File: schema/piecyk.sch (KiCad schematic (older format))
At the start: 19 parts, among them IC1 ATMEGA8A-P, Q1 PNP, SW1 SW_edit, SW2 SW_down, SW3 SW_up, U1 78L05, U2 LM35

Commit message: Correct schematics (NPN instead of PNP)
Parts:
- removed Q1: PNP, ~, symbol PNP
- added Q1: NPN, ~, symbol NPN
- added R5: R, ~, symbol R
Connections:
- net labels added: +12V / heating -
- wire segments 78 -> 82
- no-connect marks 14 -> 13
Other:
- moved on the sheet: D1, R2
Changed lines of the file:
@@
 LIBS:display_lcd
 LIBS:capteurs
-LIBS:noname-cache
 EELAYER 27 0
 EELAYER END
@@
 Vcc +5V
 $Comp
-L PNP Q1
-U 1 1 52D0DFF4
-P 6950 5500
-F 0 "Q1" H 6950 5350 60  0000 R CNN
-F 1 "PNP" H 6950 5650 60  0000 R CNN
-F 2 "~" H 6950 5500 60  0000 C CNN
-F 3 "~" H 6950 5500 60  0000 C CNN
-	1    6950 5500
-	-1   0    0    1
-$EndComp
-$Comp
 L LED D1
 U 1 1 52D0E01F
-P 7100 4700
-F 0 "D1" H 7100 4800 50  0000 C CNN
-F 1 "LED" H 7100 4600 50  0000 C CNN
-F 2 "~" H 7100 4700 60  0000 C CNN
-F 3 "~" H 7100 4700 60  0000 C CNN
-	1    7100 4700
+P 7400 4850
+F 0 "D1" H 7400 4950 50  0000 C CNN
+F 1 "LED" H 7400 4750 50  0000 C CNN
+F 2 "~" H 7400 4850 60  0000 C CNN
+F 3 "~" H 7400 4850 60  0000 C CNN
+	1    7400 4850
 	1    0    0    -1
 $EndComp
@@
 L R R2
 U 1 1 52D0E03F
-P 7300 5250
-F 0 "R2" V 7380 5250 40  0000 C CNN
-F 1 "R" V 7307 5251 40  0000 C CNN
-F 2 "~" V 7230 5250 30  0000 C CNN
-F 3 "~" H 7300 5250 30  0000 C CNN
-	1    7300 5250
+P 8200 4450
+F 0 "R2" V 8280 4450 40  0000 C CNN
+F 1 "R" V 8207 4451 40  0000 C CNN
+F 2 "~" V 8130 4450 30  0000 C CNN
+F 3 "~" H 8200 4450 30  0000 C CNN
+	1    8200 4450
 	-1   0    0    1
-$EndComp
-Text GLabel 7200 6100 2    60   Output ~ 0
-+12V piec
-$Comp
-L +12V #PWR09
-U 1 1 52D0E282
-P 6850 5100
-F 0 "#PWR09" H 6850 5050 20  0001 C CNN
-F 1 "+12V" H 6850 5200 30  0000 C CNN
-F 2 "" H 6850 5100 60  0000 C CNN
-F 3 "" H 6850 5100 60  0000 C CNN
-	1    6850 5100
-	1    0    0    -1
 $EndComp
 $Comp
@@
 $EndComp
 $Comp
-L GND #PWR010
+L GND #PWR09
 U 1 1 52D0F85C
 P 8650 2900
-F 0 "#PWR010" H 8650 2900 30  0001 C CNN
+F 0 "#PWR09" H 8650 2900 30  0001 C CNN
 F 1 "GND" H 8650 2830 30  0001 C CNN
 F 2 "" H 8650 2900 60  0000 C CNN
@@
 $EndComp
 $Comp
-L GND #PWR011
+L GND #PWR010
 U 1 1 52D0F869
 P 10550 2900
-F 0 "#PWR011" H 10550 2900 30  0001 C CNN
+F 0 "#PWR010" H 10550 2900 30  0001 C CNN
 F 1 "GND" H 10550 2830 30  0001 C CNN
 F 2 "" H 10550 2900 60  0000 C CNN
@@
 $EndComp
 $Comp
-L GND #PWR012
+L GND #PWR011
 U 1 1 52D0FAD8
 P 5750 4350
-F 0 "#PWR012" H 5750 4350 30  0001 C CNN
+F 0 "#PWR011" H 5750 4350 30  0001 C CNN
 F 1 "GND" H 5750 4280 30  0001 C CNN
 F 2 "" H 5750 4350 60  0000 C CNN
@@
 	3600 6450 3600 6600
 Wire Wire Line
-	7200 6100 6850 6100
-Wire Wire Line
-	6850 6100 6850 5700
-Wire Wire Line
-	6850 5100 6850 5300
-Wire Wire Line
-	7300 5500 7150 5500
-Wire Wire Line
 	1550 3000 6700 3000
 Wire Wire Line
@@
 Connection ~ 6450 5650
 Wire Wire Line
-	7300 4700 7300 5000
-Wire Wire Line
 	4600 5250 5250 5250
 Wire Wire Line
 	5250 5250 5250 4700
-Wire Wire Line
-	5250 4700 6900 4700
 Wire Wire Line
 	9350 2250 9350 1700
@@
 NoConn ~ 4600 4950
 NoConn ~ 4600 5050
-NoConn ~ 4600 5350
 NoConn ~ 9450 2250
 NoConn ~ 9550 2250
@@
 NoConn ~ 9750 2250
 $Comp
-L GND #PWR013
+L GND #PWR012
 U 1 1 52D0FA8D
 P 9450 6100
-F 0 "#PWR013" H 9450 6100 30  0001 C CNN
+F 0 "#PWR012" H 9450 6100 30  0001 C CNN
 F 1 "GND" H 9450 6030 30  0001 C CNN
 F 2 "" H 9450 6100 60  0000 C CNN
@@
 $EndComp
 $Comp
-L +12V #PWR014
+L +12V #PWR013
 U 1 1 52D0FA9C
 P 9650 5650
-F 0 "#PWR014" H 9650 5600 20  0001 C CNN
+F 0 "#PWR013" H 9650 5600 20  0001 C CNN
 F 1 "+12V" H 9650 5750 30  0000 C CNN
 F 2 "" H 9650 5650 60  0000 C CNN
@@
 +12V piec
 $Comp
-L PWR_FLAG #FLG015
+L PWR_FLAG #FLG014
 U 1 1 52D0FAAD
 P 9450 5700
-F 0 "#FLG015" H 9450 5795 30  0001 C CNN
+F 0 "#FLG014" H 9450 5795 30  0001 C CNN
 F 1 "PWR_FLAG" H 9450 5880 30  0000 C CNN
 F 2 "" H 9450 5700 60  0000 C CNN
@@
 $EndComp
 $Comp
-L PWR_FLAG #FLG016
+L PWR_FLAG #FLG015
 U 1 1 52D0FAC7
 P 9650 6000
-F 0 "#FLG016" H 9650 6095 30  0001 C CNN
+F 0 "#FLG015" H 9650 6095 30  0001 C CNN
 F 1 "PWR_FLAG" H 9650 6180 30  0000 C CNN
 F 2 "" H 9650 6000 60  0000 C CNN
@@
 	9450 5700 9450 6100
 $Comp
-L PWR_FLAG #FLG017
+L PWR_FLAG #FLG016
 U 1 1 52D0FB94
 P 9850 5700
-F 0 "#FLG017" H 9850 5795 30  0001 C CNN
+F 0 "#FLG016" H 9850 5795 30  0001 C CNN
 F 1 "PWR_FLAG" H 9850 5880 30  0000 C CNN
 F 2 "" H 9850 5700 60  0000 C CNN
@@
 Vcc +5v
 $Comp
-L PWR_FLAG #FLG018
+L PWR_FLAG #FLG017
 U 1 1 52D0FBFB
 P 10500 5700
-F 0 "#FLG018" H 10500 5795 30  0001 C CNN
+F 0 "#FLG017" H 10500 5795 30  0001 C CNN
 F 1 "PWR_FLAG" H 10500 5880 30  0000 C CNN
 F 2 "" H 10500 5700 60  0000 C CNN
@@
 Wire Wire Line
 	10500 5900 10350 5900
+$Comp
+L NPN Q1
+U 1 1 52D1C5B5
+P 8200 3850
+F 0 "Q1" H 8200 3700 50  0000 R CNN
+F 1 "NPN" H 8200 4000 50  0000 R CNN
+F 2 "~" H 8200 3850 60  0000 C CNN
+F 3 "~" H 8200 3850 60  0000 C CNN
+	1    8200 3850
+	0    -1   -1   0
+$EndComp
+Wire Wire Line
+	8200 4200 8200 4050
+Text GLabel 7750 3750 0    60   Input ~ 0
++12V / heating -
+Wire Wire Line
+	5250 4700 8200 4700
+Wire Wire Line
+	8000 3750 7750 3750
+$Comp
+L GND #PWR018
+U 1 1 52D1C772
+P 8750 5350
+F 0 "#PWR018" H 8750 5350 30  0001 C CNN
+F 1 "GND" H 8750 5280 30  0001 C CNN
+F 2 "" H 8750 5350 60  0000 C CNN
+F 3 "" H 8750 5350 60  0000 C CNN
+	1    8750 5350
+	1    0    0    -1
+$EndComp
+Wire Wire Line
+	8750 3750 8400 3750
+$Comp
+L R R5
+U 1 1 52D1C7DB
+P 6800 4850
+F 0 "R5" V 6880 4850 40  0000 C CNN
+F 1 "R" V 6807 4851 40  0000 C CNN
+F 2 "~" V 6730 4850 30  0000 C CNN
+F 3 "~" H 6800 4850 30  0000 C CNN
+	1    6800 4850
+	0    -1   -1   0
+$EndComp
+Wire Wire Line
+	7050 4850 7200 4850
+Wire Wire Line
+	6550 4850 5400 4850
+Wire Wire Line
+	5400 4850 5400 5350
+Wire Wire Line
+	5400 5350 4600 5350
+Wire Wire Line
+	7600 4850 8750 4850
+Connection ~ 8750 4850
+Wire Wire Line
+	8750 3750 8750 5350
 $EndSCHEMATC

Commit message: Correct capacitors
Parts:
- added C1: 100n, ~, symbol C
- C6: renamed from C5; value 100n -> 100p
- R2, R5: value R -> 150R
- R3: value R -> 2k2
- R4: value R -> 550R
- renumbered C1 to C2, C2 to C3, C3 to C4, C4 to C5
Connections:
- wire segments 82 -> 83
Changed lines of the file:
@@
 LIBS:display_lcd
 LIBS:capteurs
+LIBS:piecyk-cache
 EELAYER 27 0
 EELAYER END
@@
 Sheet 1 1
 Title "piecyk"
-Date "11 jan 2014"
+Date "12 jan 2014"
 Rev "1"
 Comp ""
@@
 $EndComp
 $Comp
-L C C1
+L C C2
 U 1 1 52BB0288
 P 2100 1400
-F 0 "C1" H 2100 1500 40  0000 L CNN
+F 0 "C2" H 2100 1500 40  0000 L CNN
 F 1 "100n" H 2106 1315 40  0000 L CNN
 F 2 "~" H 2138 1250 30  0000 C CNN
@@
 $EndComp
 $Comp
-L C C3
+L C C4
 U 1 1 52BB045F
 P 1500 4350
-F 0 "C3" H 1500 4450 40  0000 L CNN
+F 0 "C4" H 1500 4450 40  0000 L CNN
 F 1 "100n" H 1506 4265 40  0000 L CNN
 F 2 "~" H 1538 4200 30  0000 C CNN
@@
 $EndComp
 $Comp
-L C C4
+L C C5
 U 1 1 52BB046E
 P 1800 4350
-F 0 "C4" H 1800 4450 40  0000 L CNN
+F 0 "C5" H 1800 4450 40  0000 L CNN
 F 1 "100n" H 1806 4265 40  0000 L CNN
 F 2 "~" H 1838 4200 30  0000 C CNN
@@
 $EndComp
 $Comp
-L C C2
+L C C3
 U 1 1 52BB04EE
 P 3200 3200
-F 0 "C2" H 3200 3300 40  0000 L CNN
+F 0 "C3" H 3200 3300 40  0000 L CNN
 F 1 "100n" H 3206 3115 40  0000 L CNN
 F 2 "~" H 3238 3050 30  0000 C CNN
@@
 P 8200 4450
 F 0 "R2" V 8280 4450 40  0000 C CNN
-F 1 "R" V 8207 4451 40  0000 C CNN
+F 1 "150R" V 8207 4451 40  0000 C CNN
 F 2 "~" V 8130 4450 30  0000 C CNN
 F 3 "~" H 8200 4450 30  0000 C CNN
@@
 P 9050 1450
 F 0 "R3" V 9130 1450 40  0000 C CNN
-F 1 "R" V 9057 1451 40  0000 C CNN
+F 1 "2k2" V 9057 1451 40  0000 C CNN
 F 2 "~" V 8980 1450 30  0000 C CNN
 F 3 "~" H 9050 1450 30  0000 C CNN
@@
 P 10250 1450
 F 0 "R4" V 10330 1450 40  0000 C CNN
-F 1 "R" V 10257 1451 40  0000 C CNN
+F 1 "550R" V 10257 1451 40  0000 C CNN
 F 2 "~" V 10180 1450 30  0000 C CNN
 F 3 "~" H 10250 1450 30  0000 C CNN
@@
 $EndComp
 $Comp
-L C C5
+L C C6
 U 1 1 52D0FC62
 P 5750 3700
-F 0 "C5" H 5750 3800 40  0000 L CNN
-F 1 "100n" H 5756 3615 40  0000 L CNN
+F 0 "C6" H 5750 3800 40  0000 L CNN
+F 1 "100p" H 5756 3615 40  0000 L CNN
 F 2 "~" H 5788 3550 30  0000 C CNN
 F 3 "~" H 5750 3700 60  0000 C CNN
@@
 Connection ~ 5750 4000
 Wire Wire Line
-	1600 1600 2100 1600
+	1200 1600 2100 1600
 Wire Wire Line
 	6700 3000 6700 4000
@@
 P 6800 4850
 F 0 "R5" V 6880 4850 40  0000 C CNN
-F 1 "R" V 6807 4851 40  0000 C CNN
+F 1 "150R" V 6807 4851 40  0000 C CNN
 F 2 "~" V 6730 4850 30  0000 C CNN
 F 3 "~" H 6800 4850 30  0000 C CNN
@@
 Wire Wire Line
 	8750 3750 8750 5350
+$Comp
+L C C1
+U 1 1 52D1F8D5
+P 1200 1400
+F 0 "C1" H 1200 1500 40  0000 L CNN
+F 1 "100n" H 1206 1315 40  0000 L CNN
+F 2 "~" H 1238 1250 30  0000 C CNN
+F 3 "~" H 1200 1400 60  0000 C CNN
+	1    1200 1400
+	1    0    0    -1
+$EndComp
+Wire Wire Line
+	1200 1000 1200 1200
 $EndSCHEMATC

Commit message: Add PCB layout, rearrange pins a bit to clean up tracks
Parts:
- removed C6: 100p, ~, symbol C
- removed D_LCD1: DISPLAY_HD44780, symbol DISPLAY_HD44780
- added K1, K2: CONN_3, ~, symbol CONN_3
- added K3: CONN_4, ~, symbol CONN_4
- added K4, P1, P2: CONN_2, ~, symbol CONN_2
- added U3: HD44780, symbol HD44780
- Q1: value NPN -> BC517
- SW2: value SW_down -> SW_up
- SW3: value SW_up -> SW_down
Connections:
- net labels added: LCD Blight+, LCD Blight-, LCD Contr, LCD data4, LCD data5, LCD data6, LCD data7, LCD en, LCD rs, LCD rw
- net labels removed: +12V piec, LCD_db6, LCD_rw, Vcc +5v
- wire segments 83 -> 102
- no-connect marks 13 -> 9
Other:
- moved on the sheet: C1, C2, D1, Q1, R2, R3, R4, R5, SW1, SW2, SW3, U1

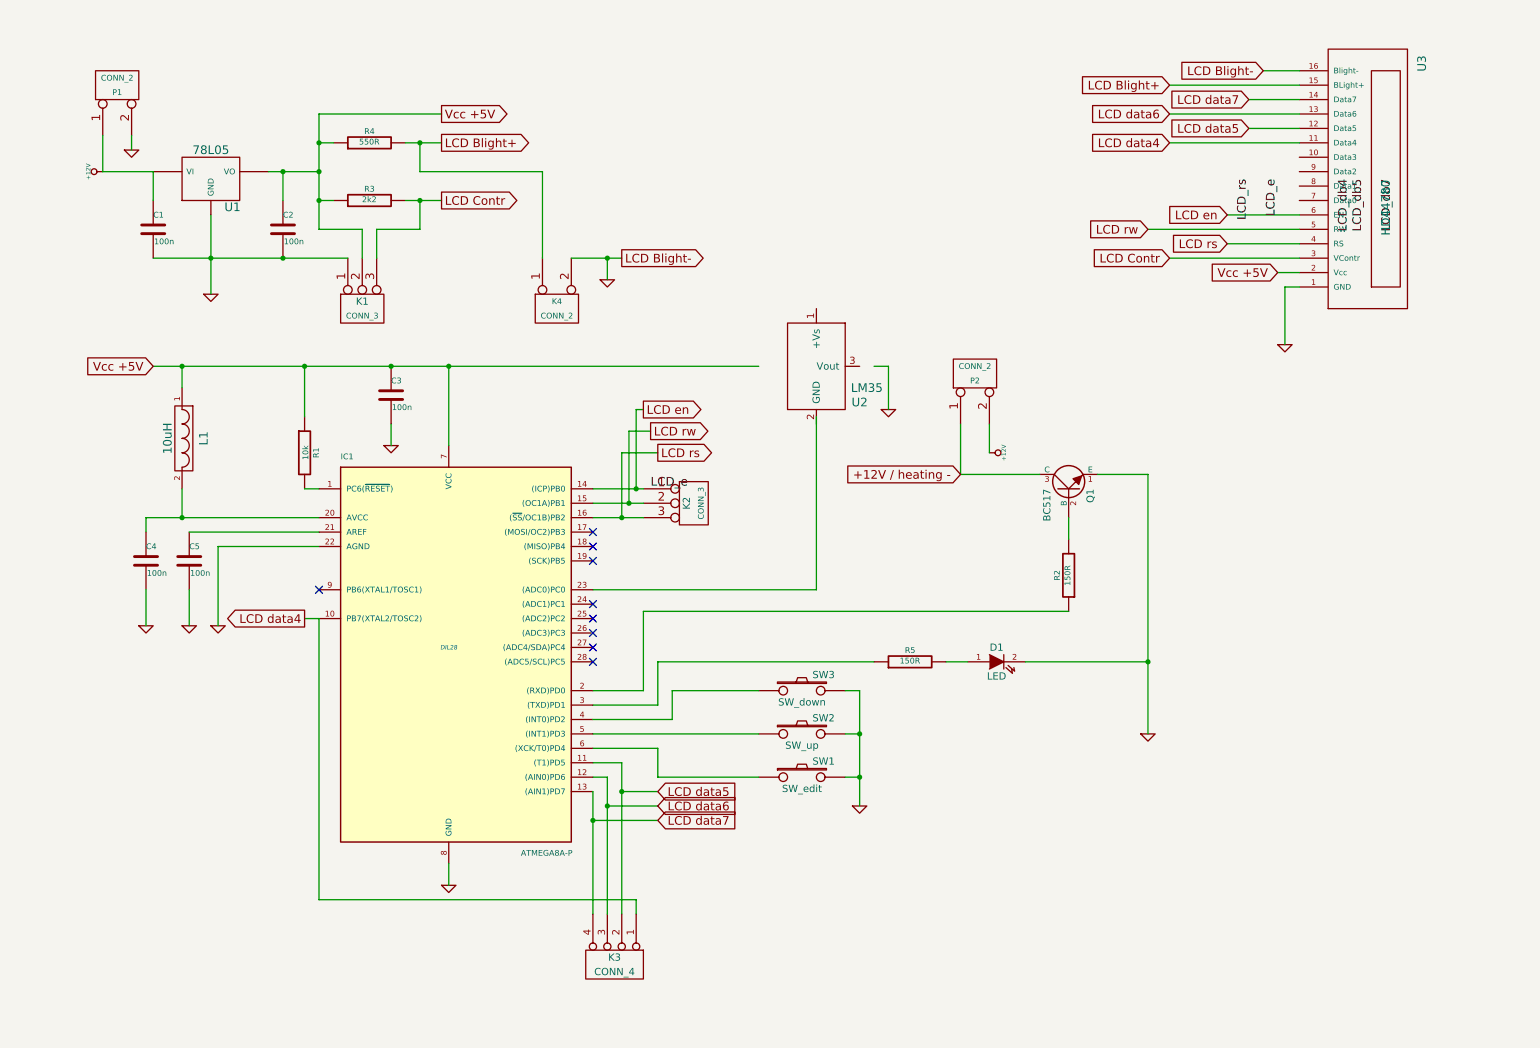
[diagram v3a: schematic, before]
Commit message: Use more compact SMD components
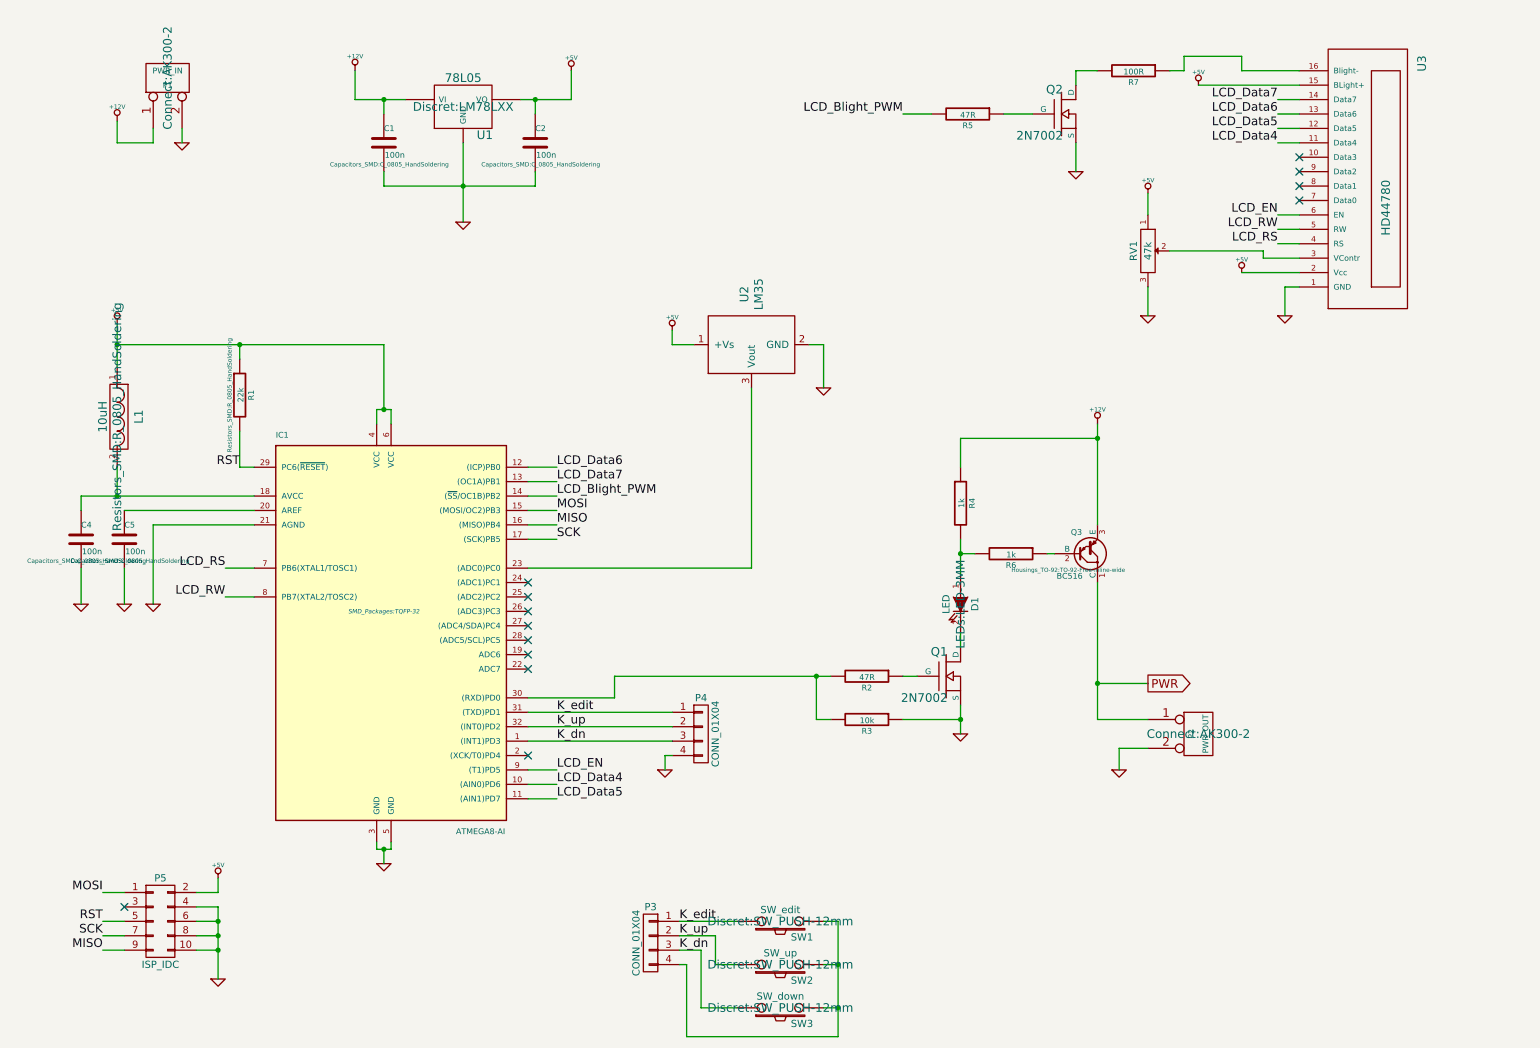
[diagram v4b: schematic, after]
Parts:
- removed C3: 100n, ~, symbol C
- removed IC1: ATMEGA8A-P, DIL28, symbol ATMEGA8A-P
- removed K1, K2: CONN_3, ~, symbol CONN_3
- removed K3: CONN_4, ~, symbol CONN_4
- removed K4: CONN_2, ~, symbol CONN_2
- removed Q1: BC517, ~, symbol NPN
- added IC1: ATMEGA8-AI, SMD_Packages:TQFP-32, symbol ATMEGA8-AI
- added P3, P4: CONN_01X04, Pin_Headers:Pin_Header_Angled_1x04, symbol CONN_01X04
- added P5: ISP_IDC, Pin_Headers:Pin_Header_Straight_2x05, symbol CONN_02X05
- added Q1, Q2: 2N7002, SMD_Packages:SOT-23-GDS, symbol MOSFET_N
- added Q3: BC516, Housings_TO-92:TO-92-Free-inline-wide, symbol BC516
- added R6: 1k, Resistors_SMD:R_0805_HandSoldering, symbol R
- added R7: 100R, Resistors_SMD:R_0805_HandSoldering, symbol R
- added RV1: 47k, Potentiometers:Potentiometer_VishaySpectrol-Econtrim-Type36P, symbol POT
- C1, C2, C4, C5: footprint ~ -> Capacitors_SMD:C_0805_HandSoldering
- D1: footprint ~ -> LEDs:LED-3MM
- L1: footprint ~ -> Resistors_SMD:R_0805_HandSoldering
- P1: value CONN_2 -> PWR_IN; footprint ~ -> Connect:AK300-2
- P2: value CONN_2 -> PWR_OUT; footprint ~ -> Connect:AK300-2
- R1: value 10k -> 22k; footprint ~ -> Resistors_SMD:R_0805_HandSoldering
- R2, R5: value 150R -> 47R; footprint ~ -> Resistors_SMD:R_0805_HandSoldering
- R3: value 2k2 -> 10k; footprint ~ -> Resistors_SMD:R_0805_HandSoldering
- R4: value 550R -> 1k; footprint ~ -> Resistors_SMD:R_0805_HandSoldering
- SW1, SW2, SW3: footprint ~ -> Discret:SW_PUSH-12mm
- U1: footprint ~ -> Discret:LM78LXX
- U2: footprint (none) -> Discret:TO92-123
- U3: footprint (none) -> Pin_Headers:Pin_Header_Straight_1x16
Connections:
- net +12V: now also R4.1, Q3.3 (E); no longer P2.2 (PM)
- net GND: now also P2.2 (PM), R3.1, U2.2 (GND), IC1.21 (AGND), IC1.3 (GND), IC1.5 (GND), P4.4 (P4), P5.10 (P10), P5.4 (P4), P5.6 (P6), P5.8 (P8), Q1.S, Q2.S, RV1.3; no longer D1.2 (K), SW1.2, SW2.2, SW3.2, U3.16 (Blight-)
- net RST: now reaches R1.2
- net RST: now also IC1.29 (PC6(~RESET~)), P5.5 (P5)
- net at C4.1, L1.2: now also IC1.18 (AVCC)
- net at C5.1: now also IC1.20 (AREF)
- net K_edit: now reaches SW1.1
- net K_edit: now also IC1.31 ((TXD)PD1), P3.1 (P1), P4.1 (P1)
- net K_up: now reaches SW2.1
- net K_up: now also IC1.32 ((INT0)PD2), P3.2 (P2), P4.2 (P2)
- net K_dn: now reaches SW3.1
- net K_dn: now also IC1.1 ((INT1)PD3), P3.3 (P3), P4.3 (P3)
- net at D1.1 (A): now also R4.2, R6.2; no longer R5.2
- net at R2.1: now also Q1.G
- net at R2.2: now also R3.2, IC1.30 ((RXD)PD0)
- net at R5.1: now also Q2.G
- net +5V: now reaches U2.1 (+Vs)
- net +5V: now also C2.1, L1.1, R1.1, U1.VO, U3.15 (BLight+), U3.2 (Vcc), IC1.4 (VCC), IC1.6 (VCC), P5.2 (P2), RV1.1
- net at U2.3 (Vout): now also IC1.23 ((ADC0)PC0)
- net +12V / heating - renamed PWR
- net PWR: now also Q3.1 (C)
- removed net LCD Blight+: R4.2, U3.15 (BLight+)
- net LCD Contr: no longer names the net of U3.3 (VContr)
- net LCD Contr: now also RV1.2; no longer R3.2
- net LCD data4 renamed LCD_Data4
- net LCD_Data4: now also IC1.10 ((AIN0)PD6)
- net LCD data5 renamed LCD_Data5
- net LCD_Data5: now also IC1.11 ((AIN1)PD7)
- net LCD data6 renamed LCD_Data6
- net LCD_Data6: now also IC1.12 ((ICP)PB0)
- net LCD data7 renamed LCD_Data7
- net LCD_Data7: now also IC1.13 ((OC1A)PB1)
- net LCD en renamed LCD_EN
- net LCD_EN: now also IC1.9 ((T1)PD5)
- net LCD rs renamed LCD_RS
- net LCD_RS: now also IC1.7 (PB6(XTAL1/TOSC1))
- net LCD rw renamed LCD_RW
- net LCD_RW: now also IC1.8 (PB7(XTAL2/TOSC2))
- removed net Vcc +5V: C2.1, L1.1, R1.1, R3.1, R4.1, U1.VO, U3.2 (Vcc)
- new net: P3.4 (P4), SW1.2, SW2.2, SW3.2
- new net: D1.2 (K), Q1.D
- new net: R7.1, U3.16 (Blight-)
- new net: Q3.2 (B), R6.1
- new net: Q2.D, R7.2
- new net LCD_Blight_PWM: IC1.14 ((~SS~/OC1B)PB2), R5.2
- new net MISO: IC1.16 ((MISO)PB4), P5.9 (P9)
- new net MOSI: IC1.15 ((MOSI/OC2)PB3), P5.1 (P1)
- new net SCK: IC1.17 ((SCK)PB5), P5.7 (P7)
- no-connect marks 9 -> 13
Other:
- moved on the sheet: C1, C2, C4, C5, D1, L1, P1, P2, R1, SW1, SW2, SW3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
